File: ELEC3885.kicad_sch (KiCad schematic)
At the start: 4 parts

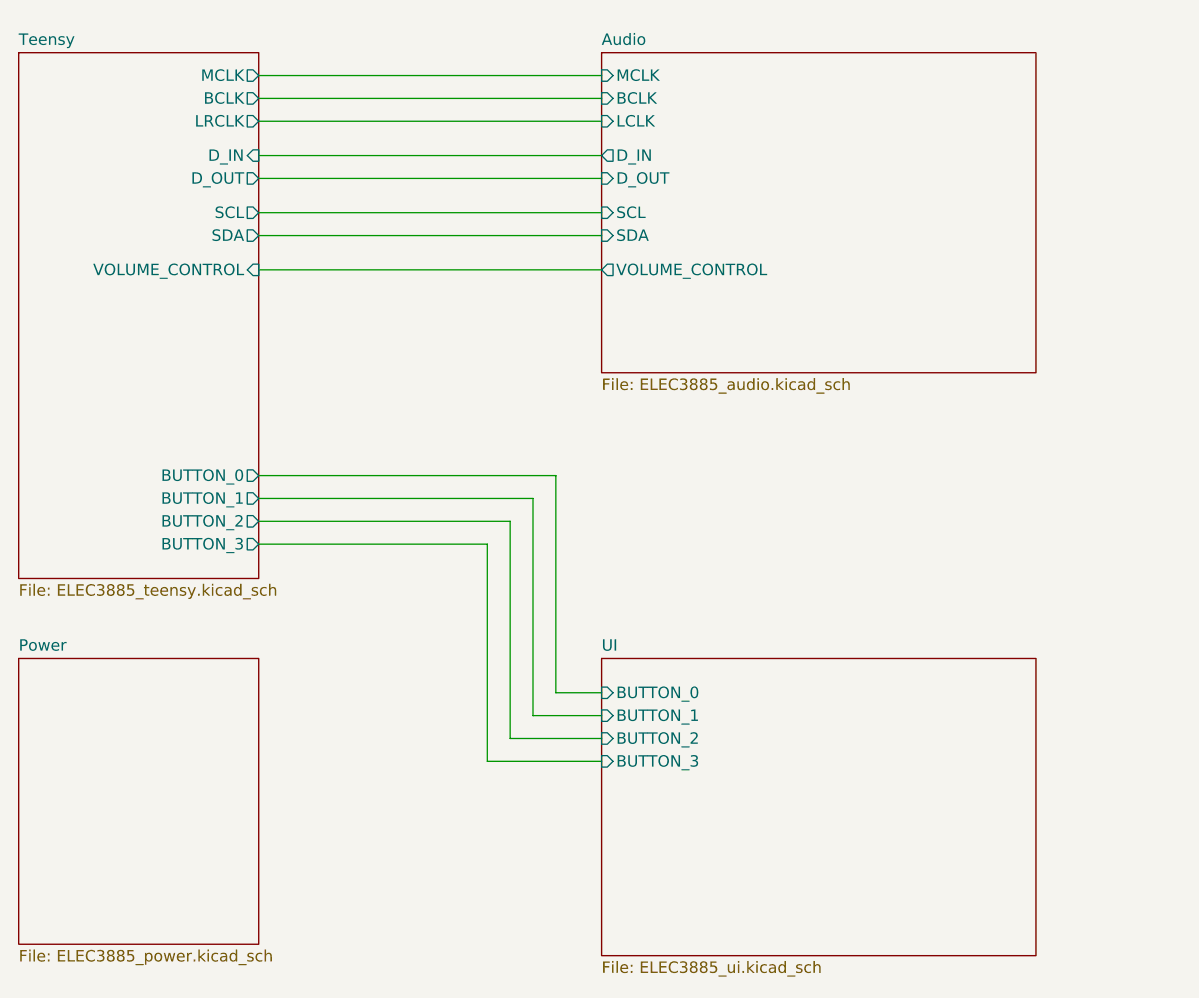
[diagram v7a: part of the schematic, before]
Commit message: Rev3 PCB layout started
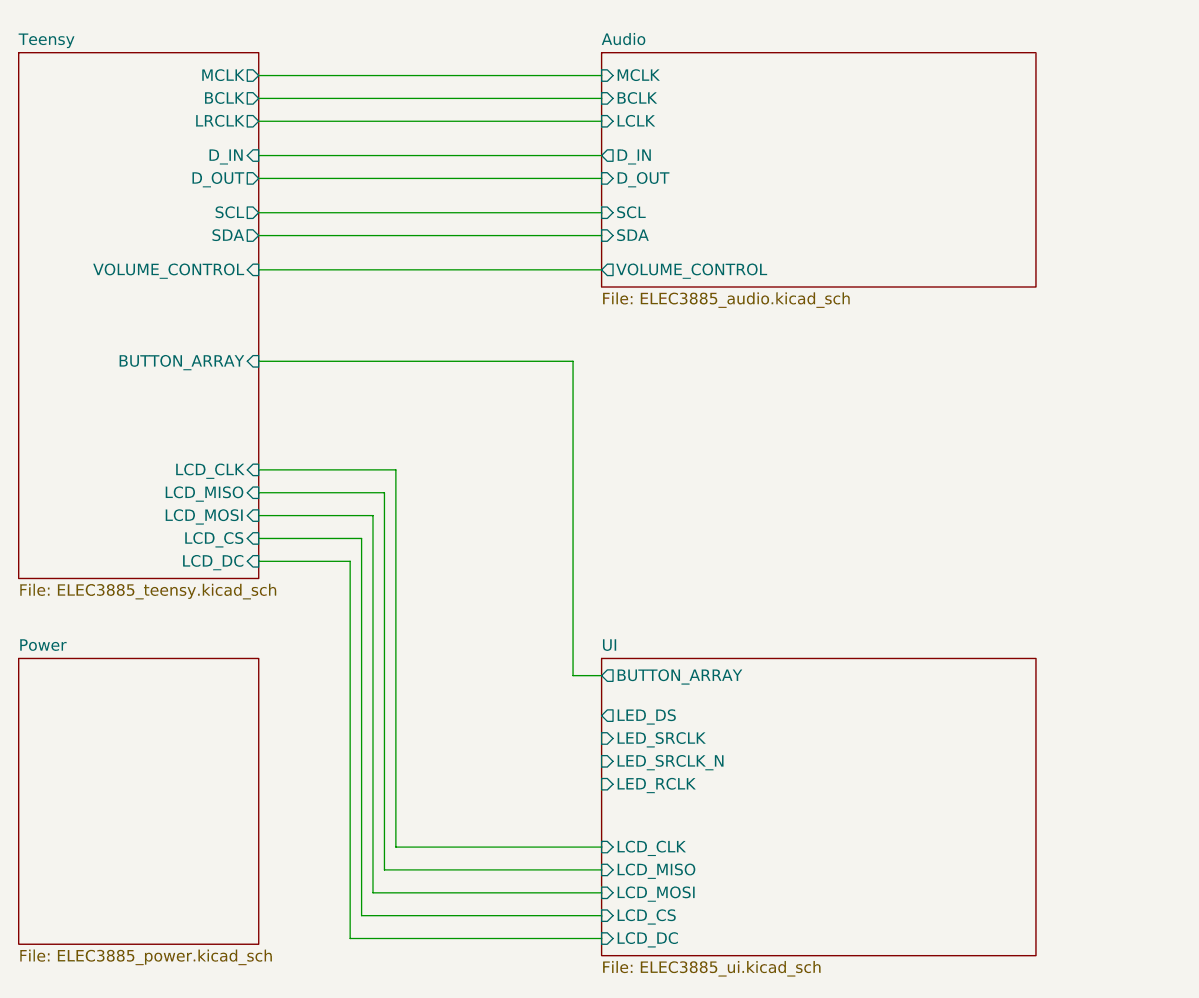
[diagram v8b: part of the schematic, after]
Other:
- sheet Teensy ports: added BUTTON_ARRAY, LCD_CLK, LCD_CS, LCD_DC, LCD_MISO, LCD_MOSI; removed BUTTON_0, BUTTON_1, BUTTON_2, BUTTON_3
- sheet UI ports: added BUTTON_ARRAY, LCD_CLK, LCD_CS, LCD_DC, LCD_MISO, LCD_MOSI, LED_DS, LED_RCLK, LED_SRCLK, LED_SRCLK_N; removed BUTTON_0, BUTTON_1, BUTTON_2, BUTTON_3
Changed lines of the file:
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@@
 (kicad_sch (version 20230121) (generator eeschema)
   (paper "A4")
+  (wire (pts (xy 77.47 90.805) (xy 87.63 90.805))
+    (stroke (width 0) (type default))
+  )
+  (wire (pts (xy 77.47 83.185) (xy 91.44 83.185))
+    (stroke (width 0) (type default))
+  )
   (wire (pts (xy 77.47 36.83) (xy 115.57 36.83))
     (stroke (width 0) (type default))
   )
-  (wire (pts (xy 115.57 105.41) (xy 110.49 105.41))
-    (stroke (width 0) (type default))
-  )
-  (wire (pts (xy 105.41 110.49) (xy 105.41 86.36))
+  (wire (pts (xy 90.17 127.635) (xy 115.57 127.635))
+    (stroke (width 0) (type default))
+  )
+  (wire (pts (xy 77.47 80.645) (xy 92.71 80.645))
+    (stroke (width 0) (type default))
+  )
+  (wire (pts (xy 77.47 88.265) (xy 88.9 88.265))
+    (stroke (width 0) (type default))
+  )
+  (wire (pts (xy 91.44 83.185) (xy 91.44 125.095))
     (stroke (width 0) (type default))
   )
@@
     (stroke (width 0) (type default))
   )
-  (wire (pts (xy 77.47 83.82) (xy 107.95 83.82))
-    (stroke (width 0) (type default))
-  )
-  (wire (pts (xy 77.47 88.9) (xy 102.87 88.9))
-    (stroke (width 0) (type default))
-  )
-  (wire (pts (xy 115.57 107.95) (xy 107.95 107.95))
+  (wire (pts (xy 112.395 68.58) (xy 112.395 103.505))
+    (stroke (width 0) (type default))
+  )
+  (wire (pts (xy 87.63 90.805) (xy 87.63 132.715))
+    (stroke (width 0) (type default))
+  )
+  (wire (pts (xy 92.71 122.555) (xy 115.57 122.555))
     (stroke (width 0) (type default))
   )
@@
     (stroke (width 0) (type default))
   )
-  (wire (pts (xy 115.57 113.03) (xy 102.87 113.03))
-    (stroke (width 0) (type default))
-  )
-  (wire (pts (xy 115.57 110.49) (xy 105.41 110.49))
+  (wire (pts (xy 77.47 68.58) (xy 112.395 68.58))
     (stroke (width 0) (type default))
   )
@@
     (stroke (width 0) (type default))
   )
-  (wire (pts (xy 102.87 113.03) (xy 102.87 88.9))
+  (wire (pts (xy 91.44 125.095) (xy 115.57 125.095))
+    (stroke (width 0) (type default))
+  )
+  (wire (pts (xy 77.47 85.725) (xy 90.17 85.725))
+    (stroke (width 0) (type default))
+  )
+  (wire (pts (xy 90.17 85.725) (xy 90.17 127.635))
+    (stroke (width 0) (type default))
+  )
+  (wire (pts (xy 112.395 103.505) (xy 115.57 103.505))
+    (stroke (width 0) (type default))
+  )
+  (wire (pts (xy 88.9 88.265) (xy 88.9 130.175))
+    (stroke (width 0) (type default))
+  )
+  (wire (pts (xy 88.9 130.175) (xy 115.57 130.175))
     (stroke (width 0) (type default))
   )
@@
     (stroke (width 0) (type default))
   )
-  (wire (pts (xy 107.95 83.82) (xy 107.95 107.95))
-    (stroke (width 0) (type default))
-  )
-  (wire (pts (xy 77.47 86.36) (xy 105.41 86.36))
-    (stroke (width 0) (type default))
-  )
-  (wire (pts (xy 77.47 81.28) (xy 110.49 81.28))
-    (stroke (width 0) (type default))
-  )
-  (wire (pts (xy 110.49 105.41) (xy 110.49 81.28))
+  (wire (pts (xy 92.71 80.645) (xy 92.71 122.555))
+    (stroke (width 0) (type default))
+  )
+  (wire (pts (xy 87.63 132.715) (xy 115.57 132.715))
     (stroke (width 0) (type default))
   )
@@
       (effects (font (size 1.27 1.27)) (justify right))
     )
-    (pin "BUTTON_0" output (at 77.47 81.28 0)
-      (effects (font (size 1.27 1.27)) (justify right))
-    )
-    (pin "BUTTON_3" output (at 77.47 88.9 0)
-      (effects (font (size 1.27 1.27)) (justify right))
-    )
-    (pin "BUTTON_1" output (at 77.47 83.82 0)
-      (effects (font (size 1.27 1.27)) (justify right))
-    )
-    (pin "BUTTON_2" output (at 77.47 86.36 0)
+    (pin "LCD_CS" input (at 77.47 88.265 0)
+      (effects (font (size 1.27 1.27)) (justify right))
+    )
+    (pin "LCD_MISO" input (at 77.47 83.185 0)
+      (effects (font (size 1.27 1.27)) (justify right))
+    )
+    (pin "LCD_MOSI" input (at 77.47 85.725 0)
+      (effects (font (size 1.27 1.27)) (justify right))
+    )
+    (pin "LCD_DC" input (at 77.47 90.805 0)
+      (effects (font (size 1.27 1.27)) (justify right))
+    )
+    (pin "LCD_CLK" input (at 77.47 80.645 0)
+      (effects (font (size 1.27 1.27)) (justify right))
+    )
+    (pin "BUTTON_ARRAY" input (at 77.47 68.58 0)
       (effects (font (size 1.27 1.27)) (justify right))
     )
@@
       (effects (font (size 1.27 1.27)) (justify left top))
     )
-    (pin "BUTTON_3" input (at 115.57 113.03 180)
-      (effects (font (size 1.27 1.27)) (justify left))
-    )
-    (pin "BUTTON_0" input (at 115.57 105.41 180)
-      (effects (font (size 1.27 1.27)) (justify left))
-    )
-    (pin "BUTTON_2" input (at 115.57 110.49 180)
-      (effects (font (size 1.27 1.27)) (justify left))
-    )
-    (pin "BUTTON_1" input (at 115.57 107.95 180)
+    (pin "BUTTON_ARRAY" output (at 115.57 103.505 180)
+      (effects (font (size 1.27 1.27)) (justify left))
+    )
+    (pin "LED_DS" output (at 115.57 107.95 180)
+      (effects (font (size 1.27 1.27)) (justify left))
+    )
+    (pin "LED_SRCLK" input (at 115.57 110.49 180)
+      (effects (font (size 1.27 1.27)) (justify left))
+    )
+    (pin "LED_SRCLK_N" input (at 115.57 113.03 180)
+      (effects (font (size 1.27 1.27)) (justify left))
+    )
+    (pin "LED_RCLK" input (at 115.57 115.57 180)
+      (effects (font (size 1.27 1.27)) (justify left))
+    )
+    (pin "LCD_CS" input (at 115.57 130.175 180)
+      (effects (font (size 1.27 1.27)) (justify left))
+    )
+    (pin "LCD_MOSI" input (at 115.57 127.635 180)
+      (effects (font (size 1.27 1.27)) (justify left))
+    )
+    (pin "LCD_DC" input (at 115.57 132.715 180)
+      (effects (font (size 1.27 1.27)) (justify left))
+    )
+    (pin "LCD_CLK" input (at 115.57 122.555 180)
+      (effects (font (size 1.27 1.27)) (justify left))
+    )
+    (pin "LCD_MISO" input (at 115.57 125.095 180)
       (effects (font (size 1.27 1.27)) (justify left))
     )
@@
     )
   )
-  (sheet (at 115.57 34.29) (size 48.26 35.56) (fields_autoplaced)
+  (sheet (at 115.57 34.29) (size 48.26 26.035) (fields_autoplaced)
     (stroke (width 0.1524) (type solid))
     (fill (color 0 0 0 0.0000))
@@
       (effects (font (size 1.27 1.27)) (justify left bottom))
     )
-    (property "Sheetfile" "ELEC3885_audio.kicad_sch" (at 115.57 70.4346 0)
-      (effects (font (size 1.27 1.27)) (justify left top))
-    )
+    (property "Sheetfile" "ELEC3885_audio.kicad_sch" (at 115.57 60.9096 0)
+      (effects (font (size 1.27 1.27)) (justify left top))
+    )
